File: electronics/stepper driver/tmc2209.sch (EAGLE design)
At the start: 61 parts, among them U1 TMC2209-LA, U2 TMC2209-LA, U3 TMC2209-LA

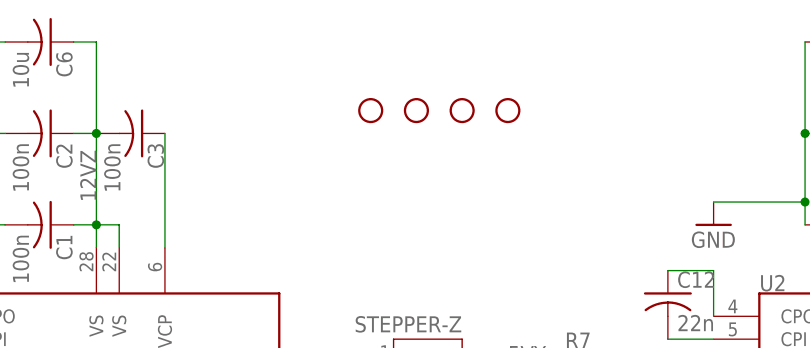
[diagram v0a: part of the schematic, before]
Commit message: updated all PCBs and added PDF schematics
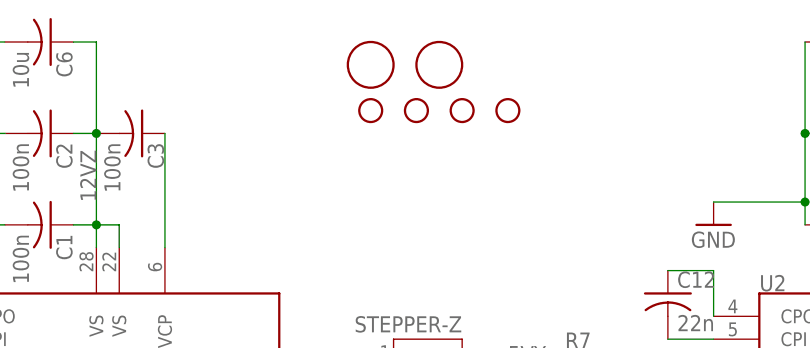
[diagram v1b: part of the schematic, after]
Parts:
- added U$1, U$2: FIDUCIAL, adafruit:FIDUCIAL
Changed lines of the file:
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@@
 <part name="STEPPER-X" library="jst-ph" deviceset="JST-PH5" device=""/>
 <part name="STEPPER-Z" library="jst-ph" deviceset="JST-PH5" device=""/>
+<part name="U$1" library="adafruit" deviceset="FIDUCIAL" device=""/>
+<part name="U$2" library="adafruit" deviceset="FIDUCIAL" device=""/>
 </parts>
 <sheets>
@@
 <attribute name="NAME" x="83.82" y="107.442" size="1.778" layer="95" rot="MR0"/>
 </instance>
+<instance part="U$1" gate="G$1" x="73.66" y="137.16"/>
+<instance part="U$2" gate="G$1" x="81.28" y="137.16"/>
 </instances>
 <busses>
